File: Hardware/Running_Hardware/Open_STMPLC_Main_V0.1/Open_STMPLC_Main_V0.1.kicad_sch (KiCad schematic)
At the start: 1 part, among them U1 STM32F407VGTx

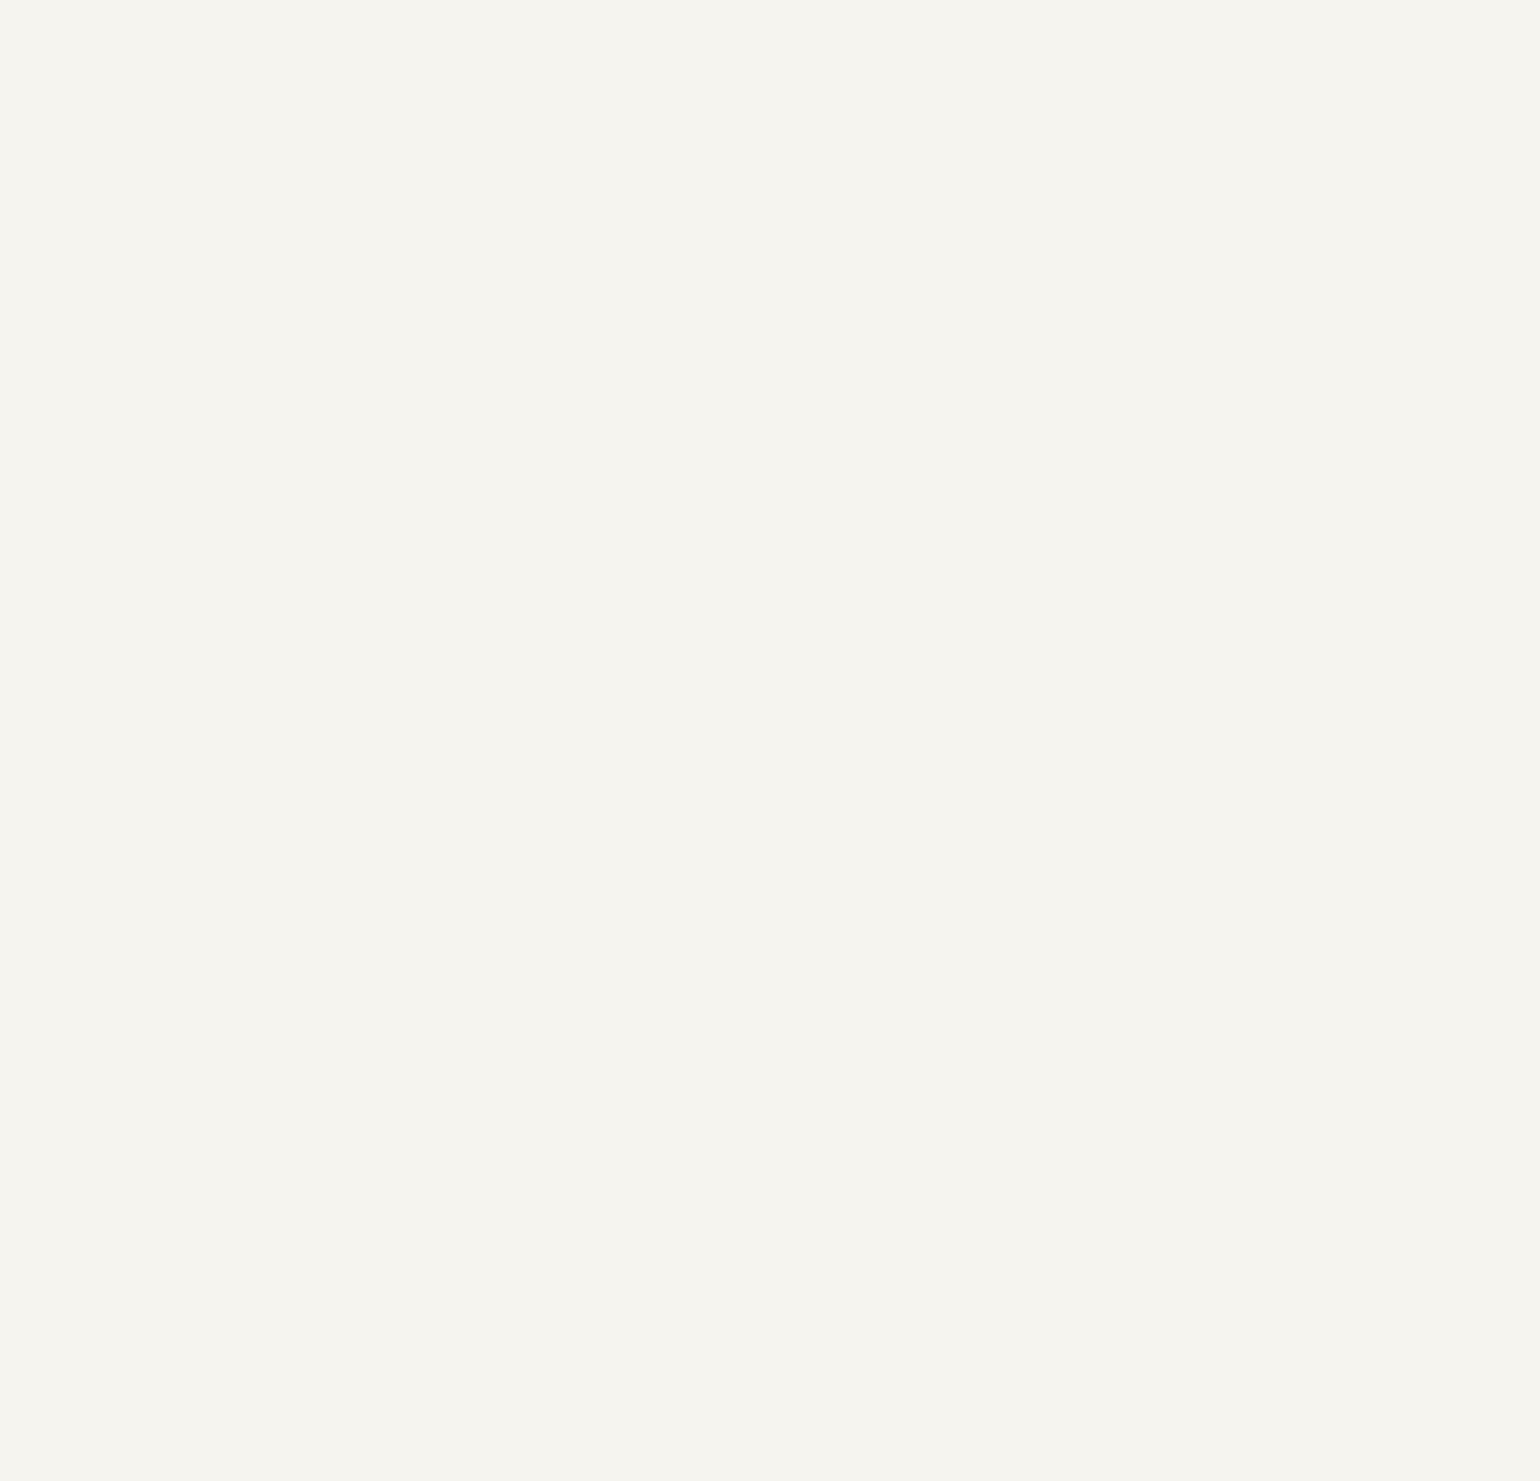
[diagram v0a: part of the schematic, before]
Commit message: Symbol libraries 1
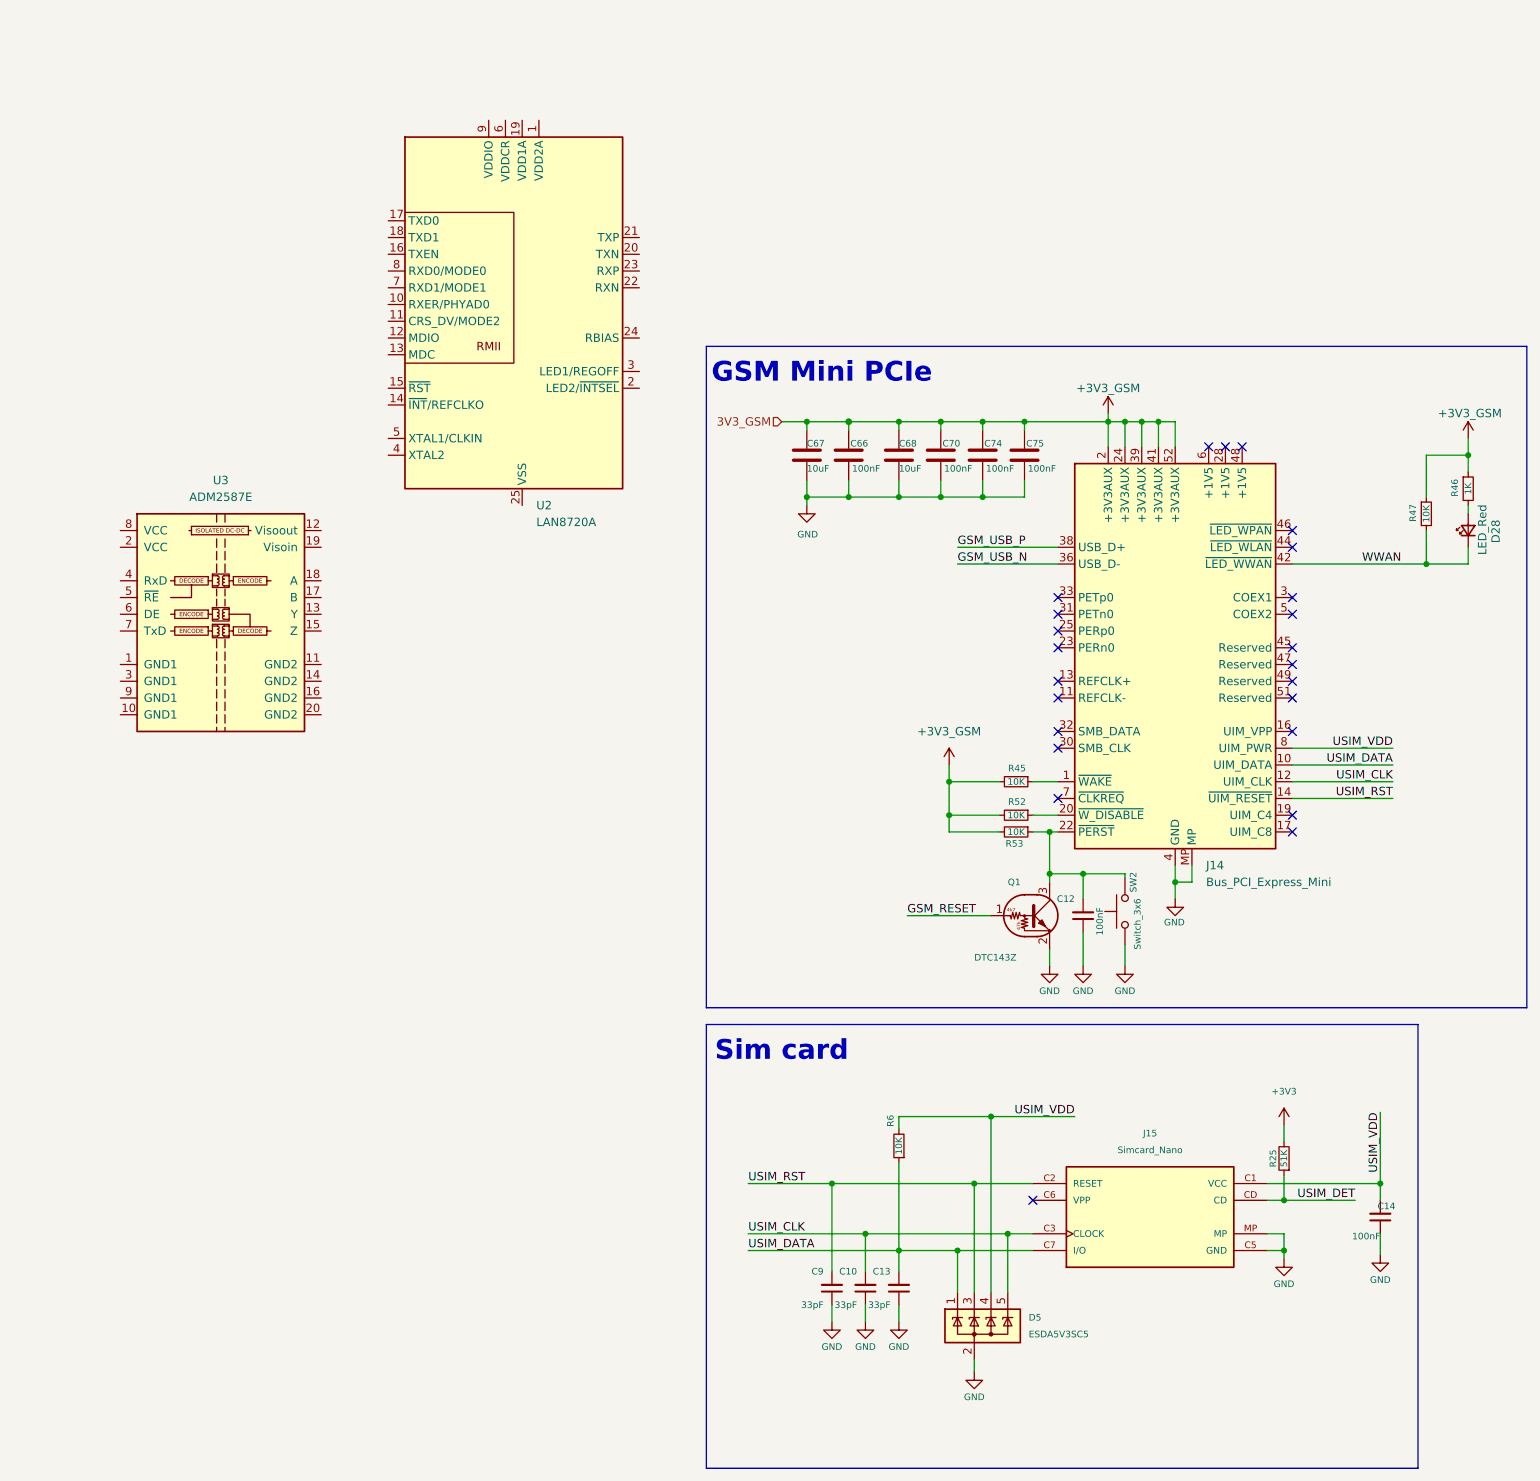
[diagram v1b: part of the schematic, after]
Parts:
- added C10, C13, C9: 33pF, Capacitor_SMD:C_0603_1608Metric_Pad1.08x0.95mm_HandSolder, symbol Device:C_Small
- added C12, C14: 100nF, Capacitor_SMD:C_0402_1005Metric_Pad0.74x0.62mm_HandSolder, symbol Device:C_Small
- added C66, C70, C74, C75: 100nF, Capacitor_SMD:C_0402_1005Metric_Pad0.74x0.62mm_HandSolder, symbol Device:C
- added C67, C68: 10uF, Capacitor_SMD:C_0603_1608Metric_Pad1.08x0.95mm_HandSolder, symbol Device:C
- added D28: LED_Red, LED_SMD:LED_0603_1608Metric, symbol Device:LED_Small
- added D5: ESDA5V3SC5, Package_TO_SOT_SMD:SOT-23-5, symbol Power_Protection:ESDA5V3SC5
- added J14: Bus_PCI_Express_Mini, Footprints:TE_1775838-2, symbol Connector:Bus_PCI_Express_Mini
- added J15: Simcard_Nano, SimCard:TE_2336582-1, symbol Simcard_Holder_Nano:47553-2001
- added Q1: DTC143Z, Package_TO_SOT_SMD:SOT-23-3, symbol Transistor_BJT:DTC143Z
- added R25: 51K, Resistor_SMD:R_0603_1608Metric_Pad0.98x0.95mm_HandSolder, symbol Device:R_Small
- added R45, R47, R52, R53, R6: 10K, Resistor_SMD:R_0603_1608Metric_Pad0.98x0.95mm_HandSolder, symbol Device:R_Small
- added R46: 1K, Resistor_SMD:R_0603_1608Metric_Pad0.98x0.95mm_HandSolder, symbol Device:R_Small
- added SW2: Switch_3x6, Button_Switch_SMD:SW_SPST_CK_RS282G05A3, symbol Switch:SW_Push
- added U2: LAN8720A, Package_DFN_QFN:VQFN-24-1EP_4x4mm_P0.5mm_EP2.5x2.5mm_ThermalVias, symbol Interface_Ethernet:LAN8720A
- added U3: ADM2587E, Package_SO:SOIC-20W_7.5x12.8mm_P1.27mm, symbol Interface_UART:ADM2587E
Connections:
- net GND: now also C10.1, C12.1, C13.1, C14.1, C66.2, C67.2, C68.2, C70.2, C74.2, C75.2, C9.1, D5.2 (A), J14.15 (GND), J14.18 (GND), J14.21 (GND), J14.26 (GND), J14.27 (GND), J14.29 (GND), J14.34 (GND), J14.35 (GND), J14.37 (GND), J14.4 (GND), J14.40 (GND), J14.43 (GND), J14.50 (GND), J14.9 (GND), J14.MP, J15.C5 (GND), J15.MP, Q1.2 (E), SW2.1
- new net: J14.1 (~{WAKE}), R45.1
- new net: J14.20 (~{W_DISABLE}), R52.1
- new net: C12.2, J14.22 (~{PERST}), Q1.3 (C), R53.1, SW2.2
- new net: D28.2 (A), R46.2
- new net +3V3: R25.2
- new net +3V3_GSM: C66.1, C67.1, C68.1, C70.1, C74.1, C75.1, J14.2 (+3V3AUX), J14.24 (+3V3AUX), J14.39 (+3V3AUX), J14.41 (+3V3AUX), J14.52 (+3V3AUX), R45.2, R46.1, R47.1, R52.2, R53.2
- new net GSM_RESET: Q1.1 (B)
- new net GSM_USB_N: J14.36 (USB_D-)
- new net GSM_USB_P: J14.38 (USB_D+)
- new net USIM_CLK: C10.2, D5.5 (K), J14.12 (UIM_CLK), J15.C3 (CLOCK)
- new net USIM_DATA: C13.2, D5.1 (K), J14.10 (UIM_DATA), J15.C7 (I/O), R6.1
- new net USIM_DET: J15.CD, R25.1
- new net USIM_RST: C9.2, D5.3 (K), J14.14 (~{UIM_RESET}), J15.C2 (RESET)
- new net USIM_VDD: C14.2, D5.4 (K), J14.8 (UIM_PWR), J15.C1 (VCC), R6.2
- new net WWAN: D28.1 (K), J14.42 (~{LED_WWAN}), R47.2
- no-connect marks 0 -> 24
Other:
- note added: "GSM Mini PCIe"
- note added: "Sim card"

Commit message: Main Schematic V0.1 updates
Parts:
- removed C12: 100nF, Capacitor_SMD:C_0402_1005Metric_Pad0.74x0.62mm_HandSolder, symbol Device:C_Small
- removed C66, C70, C74, C75: 100nF, Capacitor_SMD:C_0402_1005Metric_Pad0.74x0.62mm_HandSolder, symbol Device:C
- removed C67, C68: 10uF, Capacitor_SMD:C_0603_1608Metric_Pad1.08x0.95mm_HandSolder, symbol Device:C
- removed D28: LED_Red, LED_SMD:LED_0603_1608Metric, symbol Device:LED_Small
- removed J14: Bus_PCI_Express_Mini, Footprints:TE_1775838-2, symbol Connector:Bus_PCI_Express_Mini
- removed Q1: DTC143Z, Package_TO_SOT_SMD:SOT-23-3, symbol Transistor_BJT:DTC143Z
- removed R45, R47, R52, R53: 10K, Resistor_SMD:R_0603_1608Metric_Pad0.98x0.95mm_HandSolder, symbol Device:R_Small
- removed R46: 1K, Resistor_SMD:R_0603_1608Metric_Pad0.98x0.95mm_HandSolder, symbol Device:R_Small
- removed SW2: Switch_3x6, Button_Switch_SMD:SW_SPST_CK_RS282G05A3, symbol Switch:SW_Push
- removed U1: STM32F407VGTx, Package_QFP:LQFP-100_14x14mm_P0.5mm, symbol MCU_ST_STM32F4:STM32F407VGTx
- added C1: 100nF, symbol Device:C_Small
- added C2: 10uF, symbol Device:C_Small
- added C24, C33: 10uF, Capacitor_SMD:C_0805_2012Metric_Pad1.18x1.45mm_HandSolder, symbol Device:C_Small
- added C25, C32: 100nF, Capacitor_SMD:C_0603_1608Metric_Pad1.08x0.95mm_HandSolder, symbol Device:C_Small
- added D1, D4: SS34, symbol Device:D_Schottky_Small
- added D3: SMAJ33CA, Diode_SMD:D_SMA, symbol Diode:SMAJ33CA
- added J1: Screw_Terminal_01x02, symbol Connector:Screw_Terminal_01x02
- added J5: TF-102, Connector_Card:microSD_HC_Molex_47219-2001, symbol Connector:Micro_SD_Card
- added Q1: Q_PMOS, symbol Device:Q_PMOS
- added R1, R2: 10K, symbol Device:R_Small
- added R109, R110, R111, R112, R113, R114, R28: 10K, Resistor_SMD:R_0603_1608Metric_Pad0.98x0.95mm_HandSolder, symbol Device:R_Small
- added U5: W25Q64JVSSIQ, Package_SO:SOIC-8_5.3x5.3mm_P1.27mm, symbol Flash_Memory:W25Q64JVSSIQ
- added U6: TPD4E1U06DCKR, Package_TO_SOT_SMD:SOT-363_SC-70-6_Handsoldering, symbol TVS_Diode:TPD4E1U06DCKR
- added U7: TPS26600PWP, Package_SO:HTSSOP-16-1EP_4.4x5mm_P0.65mm_EP3.4x5mm_Mask2.66x2.46mm_ThermalVias, symbol Power_Management:TPS26600PWP
- added U8: UCC23513, Package_SO:SSO-6_6.8x4.6mm_P1.27mm_Clearance8mm, symbol UCC23153:UCC23513
- renumbered C13 to C11, C14 to C8, D5 to D2, J15 to J2, R25 to R7, U2 to U1, U3 to U4
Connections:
- net +3V3: now also C24.1, C25.1, C32.1, C33.1, J5.4 (VDD), R109.2, R110.2, R111.2, R112.2, R113.2, R114.2, R28.2, U5.8 (VCC)
- net GND: now also C1.2, C2.2, C24.2, C25.2, C32.2, C33.2, D3.2 (A2), J1.2 (Pin_2), J5.6 (VSS), J5.9 (SHIELD), U5.4 (GND), U6.2 (GND), U7.9 (GND), U8.4 (VEE)
- new net: D1.1 (K), D3.1 (A1), D4.2 (A), J1.1 (Pin_1)
- new net: C1.1, C2.1, D4.1 (K), Q1.S, R2.2, U7.15 (OUT), U7.16 (OUT), U8.6 (VCC)
- new net: D1.2 (A), Q1.D
- new net: Q1.G, R1.2, R2.1
- new net: U7.17 (RTN), U7.8 (RTN)
- new net: R1.1, U8.5 (VOUT)
- new net +24V: U7.1 (IN), U7.2 (IN)
- new net Flash_CS: R109.1, U5.1 (~{CS})
- new net Flash_Hold: R114.1, U5.7 (~{HOLD/RST}(IO3))
- new net Flash_WP: R113.1, U5.3 (~{WP}(IO2))
- new net SD_CS: J5.2 (DAT3/CD), R28.1, U6.3 (D2+)
- new net SPI2_CLK: J5.5 (CLK), R111.1, U5.6 (CLK), U6.6 (D1-)
- new net SPI2_MISO: J5.7 (DAT0), R110.1, U5.2 (DO(IO1)), U6.1 (D1+)
- new net SPI2_MOSI: J5.3 (CMD), R112.1, U5.5 (DI(IO0)), U6.4 (D2-)
- no-connect marks 24 -> 3
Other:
- added sheet Digital_Inputs (Digital_Inputs.kicad_sch)
- added sheet GSM_Module (GSM_Module.kicad_sch)
- added sheet Microcontroller (Microcontroller.kicad_sch)
- note added: "Flash Memory"
- note added: "MicroSD"
- note removed: "GSM Mini PCIe"
- moved on the sheet: C10, C11, C8, C9, D2, J2, R6, R7, U1, U4

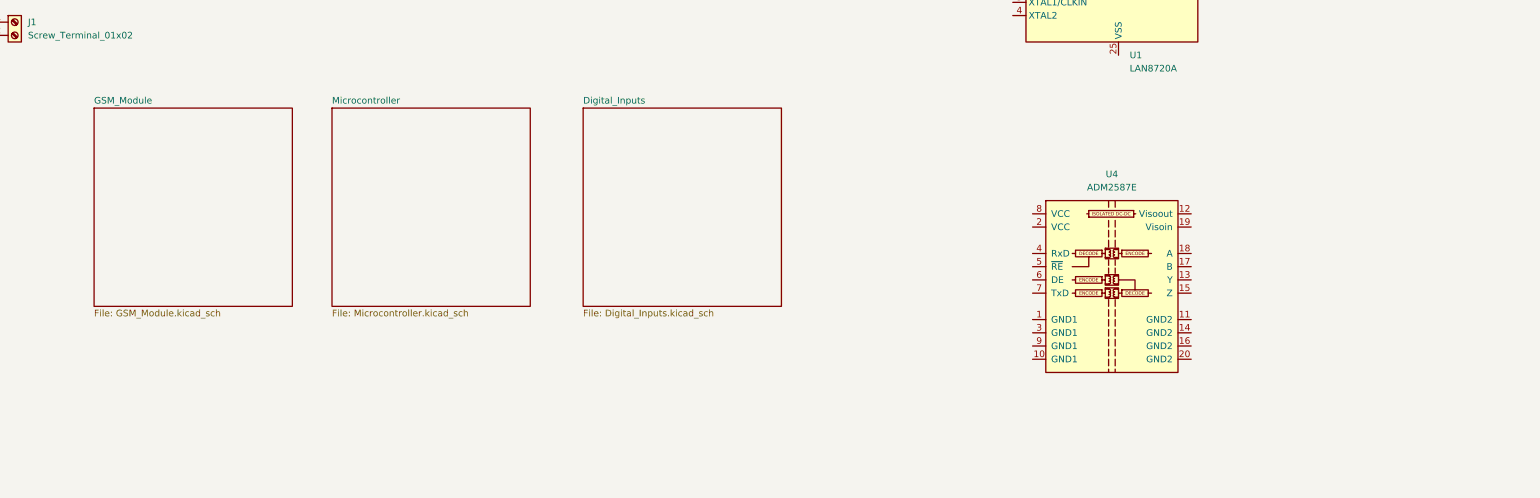
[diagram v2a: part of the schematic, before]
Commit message: MODBUS and GSM changes
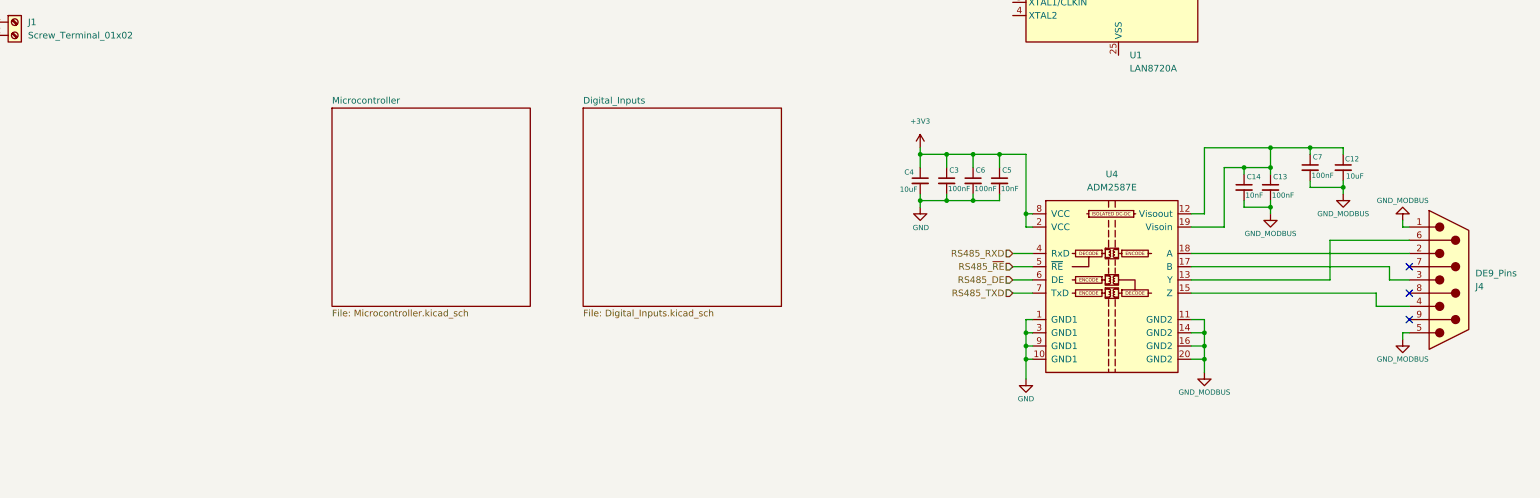
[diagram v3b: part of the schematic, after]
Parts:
- added C12, C4: 10uF, Capacitor_SMD:C_0805_2012Metric_Pad1.18x1.45mm_HandSolder, symbol Device:C_Small
- added C13, C3, C6, C7: 100nF, Capacitor_SMD:C_0603_1608Metric_Pad1.08x0.95mm_HandSolder, symbol Device:C_Small
- added C14, C5: 10nF, Capacitor_SMD:C_0603_1608Metric_Pad1.08x0.95mm_HandSolder, symbol Device:C_Small
- added J4: DE9_Pins, symbol Connector:DE9_Pins
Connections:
- net +3V3: now also U4.2 (VCC), U4.8 (VCC), C3.1, C4.1, C5.1, C6.1
- net GND: now also U4.1 (GND1), U4.10 (GND1), U4.3 (GND1), U4.9 (GND1), C3.2, C4.2, C5.2, C6.2
- net GND_MODBUS: now reaches U4.11 (GND2)
- net GND_MODBUS: now also U4.14 (GND2), U4.16 (GND2), U4.20 (GND2), C12.2, C13.2, C14.2, C7.2, J4.1, J4.5
- net at U4.12 (Visoout): now also U4.19 (Visoin), C12.1, C13.1, C14.1, C7.1
- net at U4.13 (Y): now also J4.6
- net at U4.15 (Z): now also J4.4
- net at U4.17 (B): now also J4.3
- net at U4.18 (A): now also J4.2
- net RS485_RXD: now reaches U4.4 (RxD)
- net RS485_~{RE}: now reaches U4.5 (~{RE})
- net RS485_DE: now reaches U4.6 (DE)
- net RS485_TXD: now reaches U4.7 (TxD)
- no-connect marks 3 -> 6
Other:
- removed sheet GSM_Module
